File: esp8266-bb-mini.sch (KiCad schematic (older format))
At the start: 19 parts, among them J1 Conn_01x02_Male, J2 Conn_01x04_Male, J3 Conn_01x04_Male, J4 Conn_01x04_Male, J5 Conn_01x04_Male, U1 LP38693MP-3.3, U2 ESP-12F

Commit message: stay on toplevel
Signed-off-by: Tillmann Heidsieck <theidsieck@leenox.de>
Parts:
- added H1, H2: MountingHole, MountingHole:MountingHole_3.2mm_M3, symbol Mechanical:MountingHole
- U1: symbol esp8266-bb-rescue:LP38693MP-3.3-Regulator_Linear -> Regulator_Linear:LP38693MP-3.3
- renumbered J3 to J1, J4 to J2, J5 to J3, J2 to J4, J1 to J5, R2 to R1, R3 to R2, R1 to R3, R8 to R4, R4 to R5, R5 to R6, R6 to R7, R7 to R8
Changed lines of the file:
@@
 Sheet 1 1
 Title "ESP8266 Minimal Breakout"
-Date "2020-11-30"
+Date "2020-12-02"
 Rev "1"
 Comp ""
@@
 $EndComp
 $Comp
-L Connector:Conn_01x02_Male J1
+L Connector:Conn_01x02_Male J5
 U 1 1 5FB1A223
 P 8500 2150
-F 0 "J1" H 8608 2331 50  0000 C CNN
+F 0 "J5" H 8608 2331 50  0000 C CNN
 F 1 "Conn_01x02_Male" H 8608 2240 50  0000 C CNN
 F 2 "Connector_Molex:Molex_PicoBlade_53048-0210_1x02_P1.25mm_Horizontal" H 8500 2150 50  0001 C CNN
@@
 $EndComp
 $Comp
-L esp8266-bb-rescue:LP38693MP-3.3-Regulator_Linear U1
+L Regulator_Linear:LP38693MP-3.3 U1
 U 1 1 5FB15319
 P 3250 1700
@@
 nRST
 $Comp
-L Connector:Conn_01x04_Male J3
+L Connector:Conn_01x04_Male J1
 U 1 1 5FB90F30
 P 6600 1400
-F 0 "J3" H 6708 1681 50  0000 C CNN
+F 0 "J1" H 6708 1681 50  0000 C CNN
 F 1 "Conn_01x04_Male" H 6708 1590 50  0000 C CNN
 F 2 "Connector_Molex:Molex_PicoBlade_53048-0410_1x04_P1.25mm_Horizontal" H 6600 1400 50  0001 C CNN
@@
 $EndComp
 $Comp
-L Connector:Conn_01x04_Male J5
+L Connector:Conn_01x04_Male J3
 U 1 1 5FB91C4F
 P 6600 2850
-F 0 "J5" H 6708 3131 50  0000 C CNN
+F 0 "J3" H 6708 3131 50  0000 C CNN
 F 1 "Conn_01x04_Male" H 6708 3040 50  0000 C CNN
 F 2 "Connector_Molex:Molex_PicoBlade_53048-0410_1x04_P1.25mm_Horizontal" H 6600 2850 50  0001 C CNN
@@
 $EndComp
 $Comp
-L power:+3V3 #PWR0101
+L power:+3V3 #PWR010
 U 1 1 5FB977E1
 P 6800 1500
-F 0 "#PWR0101" H 6800 1350 50  0001 C CNN
+F 0 "#PWR010" H 6800 1350 50  0001 C CNN
 F 1 "+3V3" V 6815 1628 50  0000 L CNN
 F 2 "" H 6800 1500 50  0001 C CNN
@@
 $EndComp
 $Comp
-L power:GND #PWR0102
+L power:GND #PWR011
 U 1 1 5FB977E7
 P 6800 1600
-F 0 "#PWR0102" H 6800 1350 50  0001 C CNN
+F 0 "#PWR011" H 6800 1350 50  0001 C CNN
 F 1 "GND" V 6805 1472 50  0000 R CNN
 F 2 "" H 6800 1600 50  0001 C CNN
@@
 $EndComp
 $Comp
-L power:+3V3 #PWR0103
+L power:+3V3 #PWR014
 U 1 1 5FB9DD6A
 P 6800 2950
-F 0 "#PWR0103" H 6800 2800 50  0001 C CNN
+F 0 "#PWR014" H 6800 2800 50  0001 C CNN
 F 1 "+3V3" V 6815 3078 50  0000 L CNN
 F 2 "" H 6800 2950 50  0001 C CNN
@@
 $EndComp
 $Comp
-L power:GND #PWR0104
+L power:GND #PWR015
 U 1 1 5FB9DD70
 P 6800 3050
-F 0 "#PWR0104" H 6800 2800 50  0001 C CNN
+F 0 "#PWR015" H 6800 2800 50  0001 C CNN
 F 1 "GND" V 6805 2922 50  0000 R CNN
 F 2 "" H 6800 3050 50  0001 C CNN
@@
 $EndComp
 $Comp
-L power:+3V3 #PWR0105
+L power:+3V3 #PWR012
 U 1 1 5FB9F37D
 P 6800 2200
-F 0 "#PWR0105" H 6800 2050 50  0001 C CNN
+F 0 "#PWR012" H 6800 2050 50  0001 C CNN
 F 1 "+3V3" V 6815 2328 50  0000 L CNN
 F 2 "" H 6800 2200 50  0001 C CNN
@@
 $EndComp
 $Comp
-L power:GND #PWR0106
+L power:GND #PWR013
 U 1 1 5FB9F383
 P 6800 2300
-F 0 "#PWR0106" H 6800 2050 50  0001 C CNN
+F 0 "#PWR013" H 6800 2050 50  0001 C CNN
 F 1 "GND" V 6805 2172 50  0000 R CNN
 F 2 "" H 6800 2300 50  0001 C CNN
@@
 $EndComp
 $Comp
-L Device:R R2
+L Device:R R1
 U 1 1 5FB55382
 P 3400 4300
-F 0 "R2" H 3470 4346 50  0000 L CNN
+F 0 "R1" H 3470 4346 50  0000 L CNN
 F 1 "10k" H 3470 4255 50  0000 L CNN
 F 2 "Resistor_SMD:R_0402_1005Metric" V 3330 4300 50  0001 C CNN
@@
 $EndComp
 $Comp
-L Device:R R3
+L Device:R R2
 U 1 1 5FB54C62
 P 3700 4300
-F 0 "R3" H 3770 4346 50  0000 L CNN
+F 0 "R2" H 3770 4346 50  0000 L CNN
 F 1 "10k" H 3770 4255 50  0000 L CNN
 F 2 "Resistor_SMD:R_0402_1005Metric" V 3630 4300 50  0001 C CNN
@@
 $EndComp
 $Comp
-L Device:R R5
+L Device:R R6
 U 1 1 5FB5E914
 P 5600 5600
-F 0 "R5" H 5670 5646 50  0000 L CNN
+F 0 "R6" H 5670 5646 50  0000 L CNN
 F 1 "10k" H 5670 5555 50  0000 L CNN
 F 2 "Resistor_SMD:R_0402_1005Metric" V 5530 5600 50  0001 C CNN
@@
 $EndComp
 $Comp
-L Device:R R7
+L Device:R R8
 U 1 1 5FB5A733
 P 5950 4300
-F 0 "R7" H 6020 4346 50  0000 L CNN
+F 0 "R8" H 6020 4346 50  0000 L CNN
 F 1 "10k" H 6020 4255 50  0000 L CNN
 F 2 "Resistor_SMD:R_0402_1005Metric" V 5880 4300 50  0001 C CNN
@@
 $EndComp
 $Comp
-L Device:R R6
+L Device:R R7
 U 1 1 5FB5A19C
 P 5650 4300
-F 0 "R6" H 5720 4346 50  0000 L CNN
+F 0 "R7" H 5720 4346 50  0000 L CNN
 F 1 "10k" H 5720 4255 50  0000 L CNN
 F 2 "Resistor_SMD:R_0402_1005Metric" V 5580 4300 50  0001 C CNN
@@
 $EndComp
 $Comp
-L Device:R R4
+L Device:R R5
 U 1 1 5FB599F1
 P 5350 4300
-F 0 "R4" H 5420 4346 50  0000 L CNN
+F 0 "R5" H 5420 4346 50  0000 L CNN
 F 1 "10k" H 5420 4255 50  0000 L CNN
 F 2 "Resistor_SMD:R_0402_1005Metric" V 5280 4300 50  0001 C CNN
@@
 EXT_GPIO13
 $Comp
-L Connector:Conn_01x04_Male J2
+L Connector:Conn_01x04_Male J4
 U 1 1 5FC13920
 P 8500 1350
-F 0 "J2" H 8608 1631 50  0000 C CNN
+F 0 "J4" H 8608 1631 50  0000 C CNN
 F 1 "Conn_01x04_Male" H 8608 1540 50  0000 C CNN
 F 2 "Connector_Molex:Molex_PicoBlade_53048-0410_1x04_P1.25mm_Horizontal" H 8500 1350 50  0001 C CNN
@@
 $EndComp
 $Comp
-L Connector:Conn_01x04_Male J4
+L Connector:Conn_01x04_Male J2
 U 1 1 5FB91512
 P 6600 2100
-F 0 "J4" H 6708 2381 50  0000 C CNN
+F 0 "J2" H 6708 2381 50  0000 C CNN
 F 1 "Conn_01x04_Male" H 6708 2290 50  0000 C CNN
 F 2 "Connector_Molex:Molex_PicoBlade_53048-0410_1x04_P1.25mm_Horizontal" H 6600 2100 50  0001 C CNN
@@
 	5350 4150 5650 4150
 $Comp
-L power:+BATT #PWR0107
+L power:+BATT #PWR016
 U 1 1 5FBF99E2
 P 8700 2150
-F 0 "#PWR0107" H 8700 2000 50  0001 C CNN
+F 0 "#PWR016" H 8700 2000 50  0001 C CNN
 F 1 "+BATT" H 8715 2323 50  0000 C CNN
 F 2 "" H 8700 2150 50  0001 C CNN
@@
 $EndComp
 $Comp
-L power:-BATT #PWR0108
+L power:-BATT #PWR017
 U 1 1 5FBFD1FA
 P 8700 2250
-F 0 "#PWR0108" H 8700 2100 50  0001 C CNN
+F 0 "#PWR017" H 8700 2100 50  0001 C CNN
 F 1 "-BATT" H 8715 2423 50  0000 C CNN
 F 2 "" H 8700 2250 50  0001 C CNN
@@
 $EndComp
 $Comp
-L power:PWR_FLAG #FLG0101
+L power:PWR_FLAG #FLG01
 U 1 1 5FC6F48A
 P 9000 2150
-F 0 "#FLG0101" H 9000 2225 50  0001 C CNN
+F 0 "#FLG01" H 9000 2225 50  0001 C CNN
 F 1 "PWR_FLAG" H 9000 2323 50  0000 C CNN
 F 2 "" H 9000 2150 50  0001 C CNN
@@
 Connection ~ 8700 2150
 $Comp
-L power:PWR_FLAG #FLG0102
+L power:PWR_FLAG #FLG02
 U 1 1 5FC71955
 P 9000 2250
-F 0 "#FLG0102" H 9000 2325 50  0001 C CNN
+F 0 "#FLG02" H 9000 2325 50  0001 C CNN
 F 1 "PWR_FLAG" H 9000 2423 50  0000 C CNN
 F 2 "" H 9000 2250 50  0001 C CNN
@@
 ADC_IN
 $Comp
-L power:+BATT #PWR0109
+L power:+BATT #PWR08
 U 1 1 5FC71883
 P 5050 2100
-F 0 "#PWR0109" H 5050 1950 50  0001 C CNN
+F 0 "#PWR08" H 5050 1950 50  0001 C CNN
 F 1 "+BATT" H 5065 2273 50  0000 C CNN
 F 2 "" H 5050 2100 50  0001 C CNN
@@
 $EndComp
 $Comp
-L power:-BATT #PWR0110
+L power:-BATT #PWR09
 U 1 1 5FC72393
 P 5050 2900
-F 0 "#PWR0110" H 5050 2750 50  0001 C CNN
+F 0 "#PWR09" H 5050 2750 50  0001 C CNN
 F 1 "-BATT" H 5065 3073 50  0000 C CNN
 F 2 "" H 5050 2900 50  0001 C CNN
@@
 	5050 2500 5050 2600
 $Comp
-L Device:R R8
+L Device:R R4
 U 1 1 5FC6DF52
 P 5050 2750
-F 0 "R8" H 5120 2796 50  0000 L CNN
+F 0 "R4" H 5120 2796 50  0000 L CNN
 F 1 "9k" H 5120 2705 50  0000 L CNN
 F 2 "Resistor_SMD:R_0402_1005Metric" V 4980 2750 50  0001 C CNN
@@
 $EndComp
 $Comp
-L Device:R R1
+L Device:R R3
 U 1 1 5FC6F0BF
 P 5050 2250
-F 0 "R1" H 5120 2296 50  0000 L CNN
+F 0 "R3" H 5120 2296 50  0000 L CNN
 F 1 "47k" H 5120 2205 50  0000 L CNN
 F 2 "Resistor_SMD:R_0402_1005Metric" V 4980 2250 50  0001 C CNN
@@
 	1    0    0    -1
 $EndComp
+$Comp
+L Mechanical:MountingHole H1
+U 1 1 5FC7B6C1
+P 1200 6900
+F 0 "H1" H 1300 6946 50  0000 L CNN
+F 1 "MountingHole" H 1300 6855 50  0000 L CNN
+F 2 "MountingHole:MountingHole_3.2mm_M3" H 1200 6900 50  0001 C CNN
+F 3 "~" H 1200 6900 50  0001 C CNN
+	1    1200 6900
+	1    0    0    -1
+$EndComp
+$Comp
+L Mechanical:MountingHole H2
+U 1 1 5FC7BE96
+P 1200 7200
+F 0 "H2" H 1300 7246 50  0000 L CNN
+F 1 "MountingHole" H 1300 7155 50  0000 L CNN
+F 2 "MountingHole:MountingHole_3.2mm_M3" H 1200 7200 50  0001 C CNN
+F 3 "~" H 1200 7200 50  0001 C CNN
+	1    1200 7200
+	1    0    0    -1
+$EndComp

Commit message: schematic: reduce mounting holes to m2.5, change type to with pad on top
Signed-off-by: Tillmann Heidsieck <theidsieck@leenox.de>
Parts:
- H1, H2: footprint MountingHole:MountingHole_3.2mm_M3 -> MountingHole:MountingHole_2.7mm_M2.5_DIN965_Pad_TopOnly
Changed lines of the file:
@@
 F 0 "H1" H 1300 6946 50  0000 L CNN
 F 1 "MountingHole" H 1300 6855 50  0000 L CNN
-F 2 "MountingHole:MountingHole_3.2mm_M3" H 1200 6900 50  0001 C CNN
+F 2 "MountingHole:MountingHole_2.7mm_M2.5_DIN965_Pad_TopOnly" H 1200 6900 50  0001 C CNN
 F 3 "~" H 1200 6900 50  0001 C CNN
 	1    1200 6900
@@
 F 0 "H2" H 1300 7246 50  0000 L CNN
 F 1 "MountingHole" H 1300 7155 50  0000 L CNN
-F 2 "MountingHole:MountingHole_3.2mm_M3" H 1200 7200 50  0001 C CNN
+F 2 "MountingHole:MountingHole_2.7mm_M2.5_DIN965_Pad_TopOnly" H 1200 7200 50  0001 C CNN
 F 3 "~" H 1200 7200 50  0001 C CNN
 	1    1200 7200

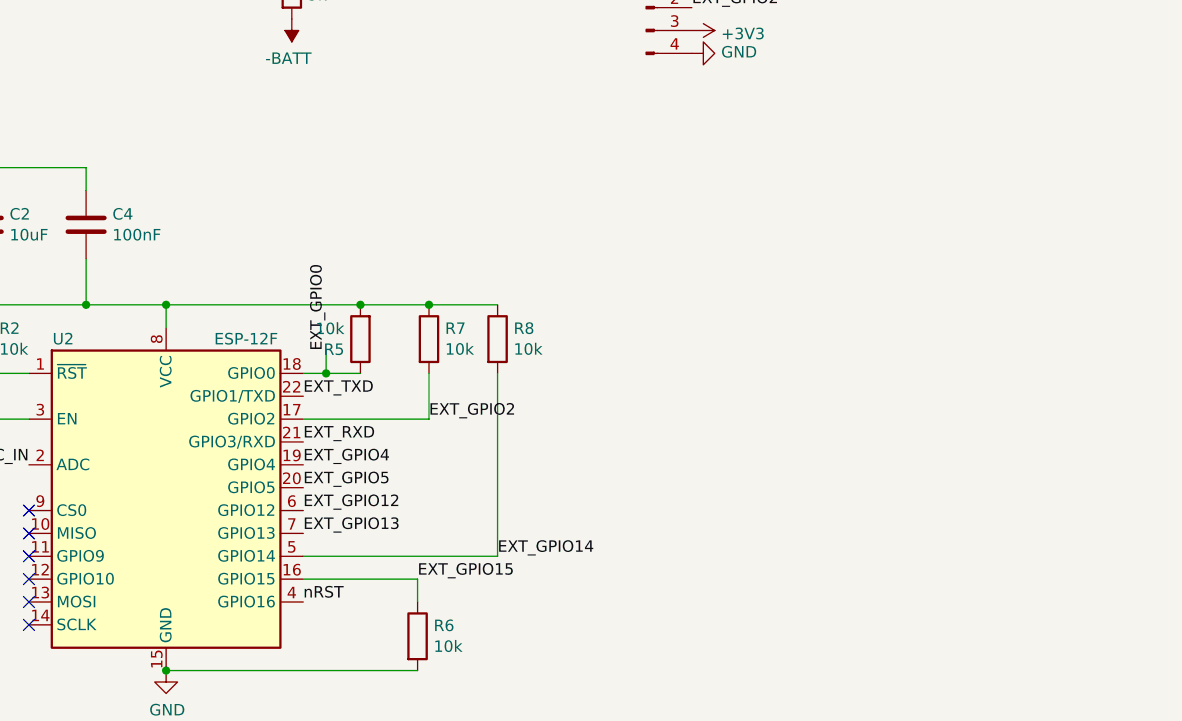
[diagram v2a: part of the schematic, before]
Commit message: add pull-ups for all gpios
Signed-off-by: Tillmann Heidsieck <theidsieck@leenox.de>
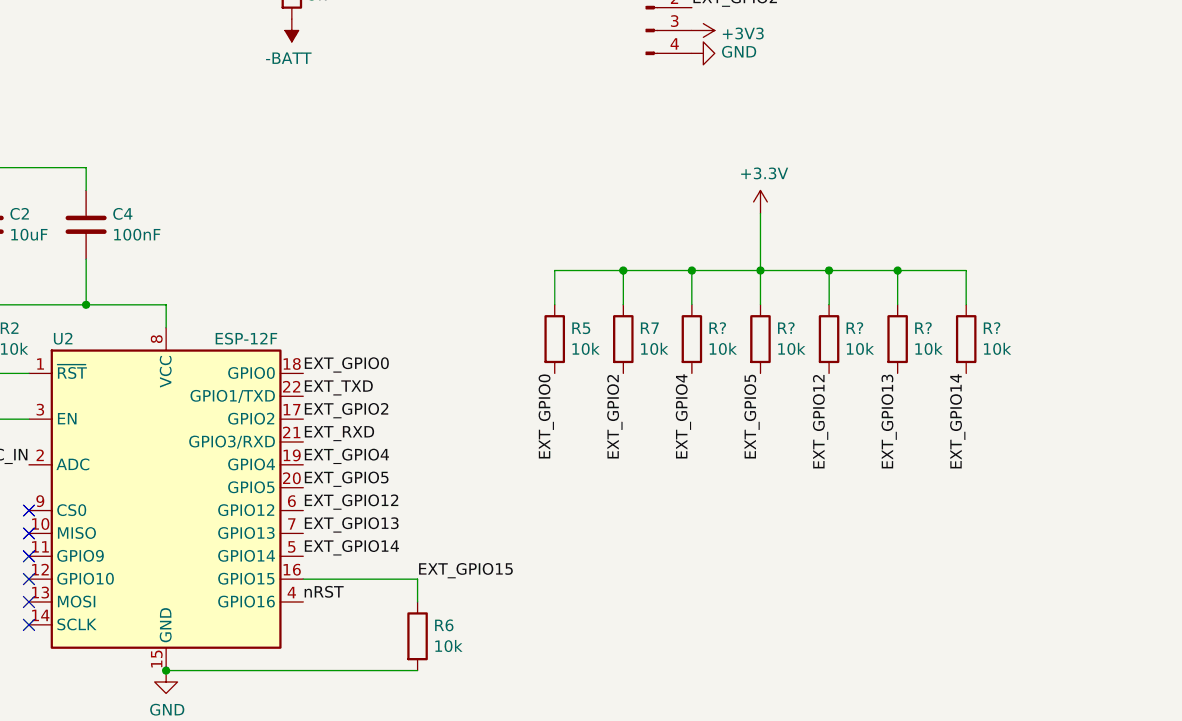
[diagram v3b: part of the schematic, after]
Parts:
- removed R8: 10k, Resistor_SMD:R_0402_1005Metric, symbol Device:R
- added R? (x5): 10k, Resistor_SMD:R_0402_1005Metric, symbol Device:R
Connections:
- net +3V3: now also R5.1, R?.1, R?.1, R?.1, R?.1, R?.1; no longer R5.2
- net EXT_GPIO0: now also R5.2; no longer R5.1
- net EXT_GPIO12: now also R?.2
- net EXT_GPIO13: now also R?.2
- net EXT_GPIO14: now also R?.2
- net EXT_GPIO4: now also R?.2
- net EXT_GPIO5: now also R?.2
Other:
- moved on the sheet: R5, R7
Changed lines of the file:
@@
 Wire Wire Line
 	3400 4650 3400 4450
-Connection ~ 4500 4150
-Connection ~ 5650 4150
-Wire Wire Line
-	5650 4150 5950 4150
-Wire Wire Line
-	5350 4450 5200 4450
-Wire Wire Line
-	5650 4650 5650 4450
-Wire Wire Line
-	5100 5250 5950 5250
-Wire Wire Line
-	5950 5250 5950 4450
 Wire Wire Line
 	5100 5350 5600 5350
 Wire Wire Line
 	5600 5350 5600 5450
-Wire Wire Line
-	5200 4450 5200 4350
-Connection ~ 5200 4450
-Wire Wire Line
-	5200 4450 5100 4450
-Text Label 5200 4350 1    50   ~ 0
+Text Label 5100 4450 0    50   ~ 0
 EXT_GPIO0
 Text Label 5100 4550 0    50   ~ 0
@@
 Text Label 5100 4750 0    50   ~ 0
 EXT_RXD
-Text Label 5100 4850 0    50   ~ 0
-EXT_GPIO4
-Text Label 5100 4950 0    50   ~ 0
-EXT_GPIO5
-Text Label 5100 5050 0    50   ~ 0
-EXT_GPIO12
 Text Label 5100 5150 0    50   ~ 0
 EXT_GPIO13
-Text Label 5650 4650 0    50   ~ 0
+Text Label 5100 4650 0    50   ~ 0
 EXT_GPIO2
-Wire Wire Line
-	5100 4650 5650 4650
-Text Label 5950 5250 0    50   ~ 0
+Text Label 5100 5250 0    50   ~ 0
 EXT_GPIO14
 Text Label 5600 5350 0    50   ~ 0
@@
 $EndComp
 $Comp
-L Device:R R8
-U 1 1 5FB5A733
-P 5950 4300
-F 0 "R8" H 6020 4346 50  0000 L CNN
-F 1 "10k" H 6020 4255 50  0000 L CNN
-F 2 "Resistor_SMD:R_0402_1005Metric" V 5880 4300 50  0001 C CNN
-F 3 "~" H 5950 4300 50  0001 C CNN
-	1    5950 4300
-	1    0    0    -1
-$EndComp
-$Comp
 L Device:R R7
 U 1 1 5FB5A19C
-P 5650 4300
-F 0 "R7" H 5720 4346 50  0000 L CNN
-F 1 "10k" H 5720 4255 50  0000 L CNN
-F 2 "Resistor_SMD:R_0402_1005Metric" V 5580 4300 50  0001 C CNN
-F 3 "~" H 5650 4300 50  0001 C CNN
-	1    5650 4300
+P 6500 4300
+F 0 "R7" H 6570 4346 50  0000 L CNN
+F 1 "10k" H 6570 4255 50  0000 L CNN
+F 2 "Resistor_SMD:R_0402_1005Metric" V 6430 4300 50  0001 C CNN
+F 3 "~" H 6500 4300 50  0001 C CNN
+	1    6500 4300
 	1    0    0    -1
 $EndComp
@@
 L Device:R R5
 U 1 1 5FB599F1
-P 5350 4300
-F 0 "R5" H 5420 4346 50  0000 L CNN
-F 1 "10k" H 5420 4255 50  0000 L CNN
-F 2 "Resistor_SMD:R_0402_1005Metric" V 5280 4300 50  0001 C CNN
-F 3 "~" H 5350 4300 50  0001 C CNN
-	1    5350 4300
-	-1   0    0    1
+P 6200 4300
+F 0 "R5" H 6270 4346 50  0000 L CNN
+F 1 "10k" H 6270 4255 50  0000 L CNN
+F 2 "Resistor_SMD:R_0402_1005Metric" V 6130 4300 50  0001 C CNN
+F 3 "~" H 6200 4300 50  0001 C CNN
+	1    6200 4300
+	1    0    0    -1
 $EndComp
 Text Label 6800 1300 0    50   ~ 0
@@
 	1    0    0    -1
 $EndComp
-Wire Wire Line
-	4500 4150 5350 4150
-Connection ~ 5350 4150
-Wire Wire Line
-	5350 4150 5650 4150
 $Comp
 L power:+BATT #PWR016
@@
 	1    0    0    -1
 $EndComp
+Text Label 5100 4850 0    50   ~ 0
+EXT_GPIO4
+Text Label 5100 4950 0    50   ~ 0
+EXT_GPIO5
+Text Label 5100 5050 0    50   ~ 0
+EXT_GPIO12
+$Comp
+L Device:R R?
+U 1 1 5FED4C62
+P 6800 4300
+F 0 "R?" H 6870 4346 50  0000 L CNN
+F 1 "10k" H 6870 4255 50  0000 L CNN
+F 2 "Resistor_SMD:R_0402_1005Metric" V 6730 4300 50  0001 C CNN
+F 3 "~" H 6800 4300 50  0001 C CNN
+	1    6800 4300
+	1    0    0    -1
+$EndComp
+$Comp
+L Device:R R?
+U 1 1 5FED53C5
+P 7100 4300
+F 0 "R?" H 7170 4346 50  0000 L CNN
+F 1 "10k" H 7170 4255 50  0000 L CNN
+F 2 "Resistor_SMD:R_0402_1005Metric" V 7030 4300 50  0001 C CNN
+F 3 "~" H 7100 4300 50  0001 C CNN
+	1    7100 4300
+	1    0    0    -1
+$EndComp
+$Comp
+L Device:R R?
+U 1 1 5FED6300
+P 7400 4300
+F 0 "R?" H 7470 4346 50  0000 L CNN
+F 1 "10k" H 7470 4255 50  0000 L CNN
+F 2 "Resistor_SMD:R_0402_1005Metric" V 7330 4300 50  0001 C CNN
+F 3 "~" H 7400 4300 50  0001 C CNN
+	1    7400 4300
+	1    0    0    -1
+$EndComp
+$Comp
+L Device:R R?
+U 1 1 5FED6B2D
+P 7700 4300
+F 0 "R?" H 7770 4346 50  0000 L CNN
+F 1 "10k" H 7770 4255 50  0000 L CNN
+F 2 "Resistor_SMD:R_0402_1005Metric" V 7630 4300 50  0001 C CNN
+F 3 "~" H 7700 4300 50  0001 C CNN
+	1    7700 4300
+	1    0    0    -1
+$EndComp
+$Comp
+L Device:R R?
+U 1 1 5FED7182
+P 8000 4300
+F 0 "R?" H 8070 4346 50  0000 L CNN
+F 1 "10k" H 8070 4255 50  0000 L CNN
+F 2 "Resistor_SMD:R_0402_1005Metric" V 7930 4300 50  0001 C CNN
+F 3 "~" H 8000 4300 50  0001 C CNN
+	1    8000 4300
+	1    0    0    -1
+$EndComp
+Text Label 6200 4450 3    50   ~ 0
+EXT_GPIO0
+Text Label 6500 4450 3    50   ~ 0
+EXT_GPIO2
+Text Label 6800 4450 3    50   ~ 0
+EXT_GPIO4
+Text Label 7100 4450 3    50   ~ 0
+EXT_GPIO5
+Text Label 7400 4450 3    50   ~ 0
+EXT_GPIO12
+Text Label 7700 4450 3    50   ~ 0
+EXT_GPIO13
+Text Label 8000 4450 3    50   ~ 0
+EXT_GPIO14
+Wire Wire Line
+	6200 4150 6200 4000
+Wire Wire Line
+	8000 4000 8000 4150
+Wire Wire Line
+	7700 4150 7700 4000
+Connection ~ 7700 4000
+Wire Wire Line
+	7700 4000 8000 4000
+Wire Wire Line
+	7400 4150 7400 4000
+Connection ~ 7400 4000
+Wire Wire Line
+	7400 4000 7700 4000
+Wire Wire Line
+	7100 4150 7100 4000
+Connection ~ 7100 4000
+Wire Wire Line
+	7100 4000 7400 4000
+Wire Wire Line
+	6800 4150 6800 4000
+Wire Wire Line
+	6200 4000 6500 4000
+Connection ~ 6800 4000
+Wire Wire Line
+	6800 4000 7100 4000
+Wire Wire Line
+	6500 4150 6500 4000
+Connection ~ 6500 4000
+Wire Wire Line
+	6500 4000 6800 4000
+Wire Wire Line
+	7100 4000 7100 3750
+$Comp
+L power:+3.3V #PWR?
+U 1 1 5FEDEC55
+P 7100 3750
+F 0 "#PWR?" H 7100 3600 50  0001 C CNN
+F 1 "+3.3V" H 7115 3923 50  0000 C CNN
+F 2 "" H 7100 3750 50  0001 C CNN
+F 3 "" H 7100 3750 50  0001 C CNN
+	1    7100 3750
+	1    0    0    -1
+$EndComp
